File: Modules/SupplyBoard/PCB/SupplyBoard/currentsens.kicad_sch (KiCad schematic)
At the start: 8 parts

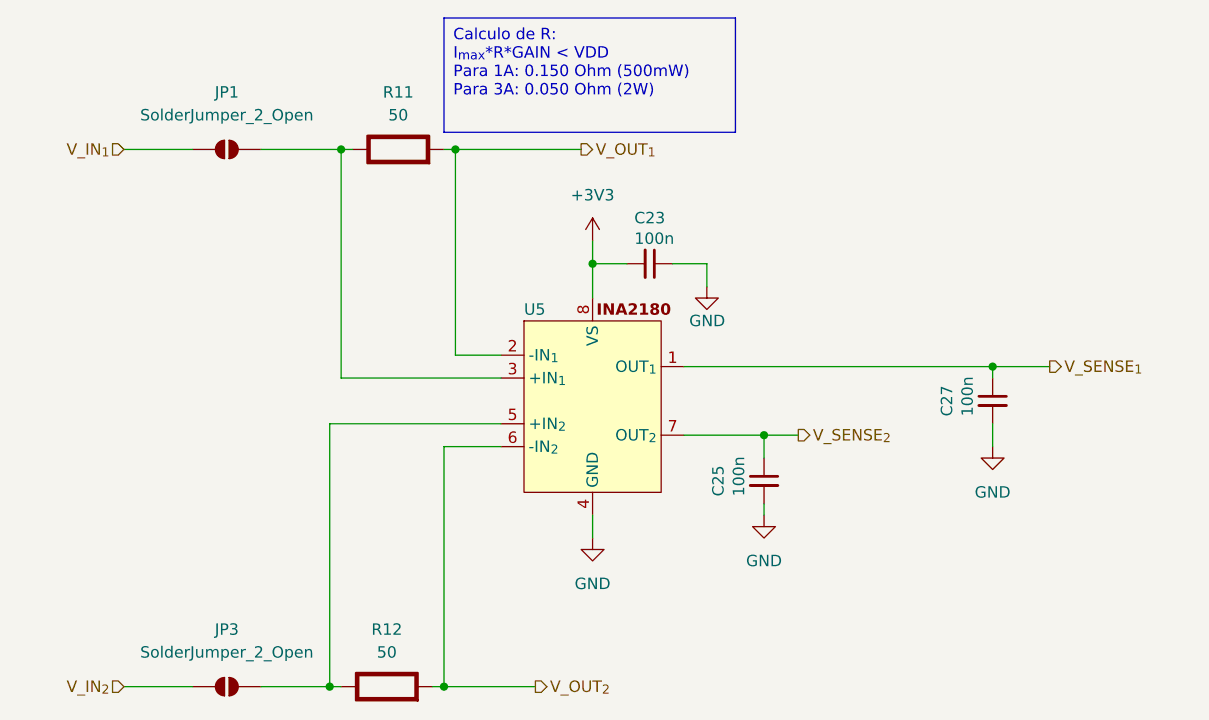
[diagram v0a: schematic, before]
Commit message: Supply board schematic and PCB
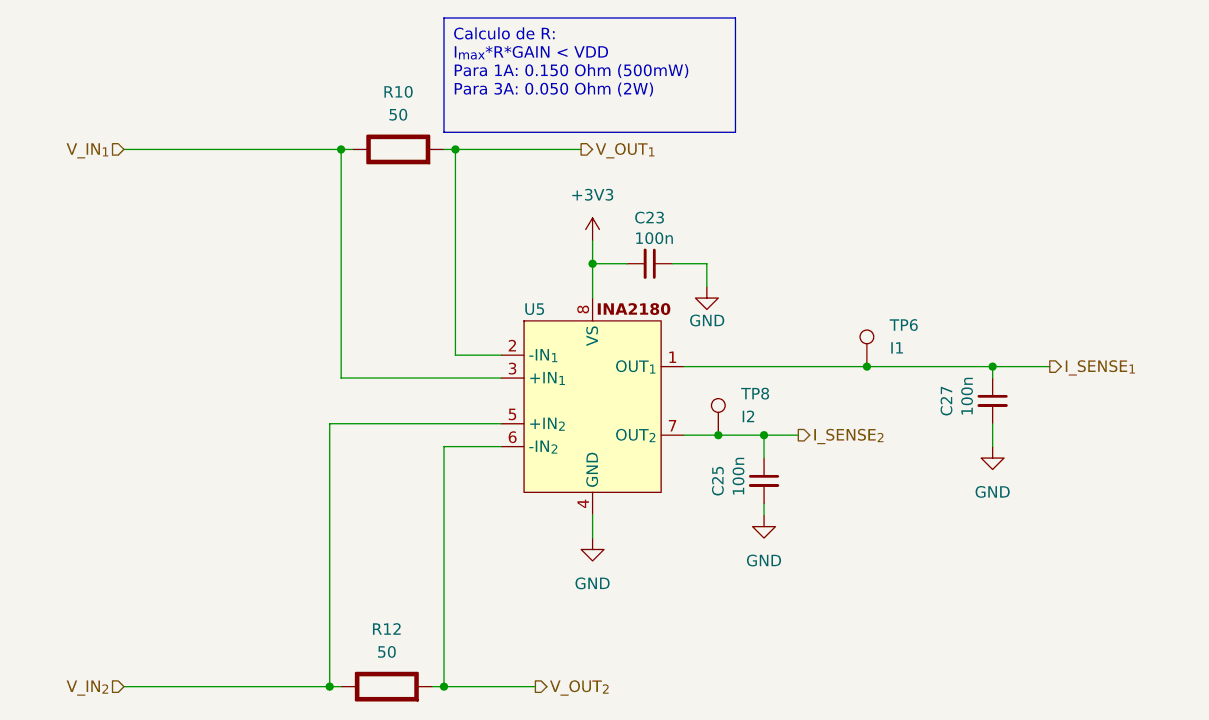
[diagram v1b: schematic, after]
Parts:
- removed JP1, JP3: SolderJumper_2_Open, Jumper:SolderJumper-2_P1.3mm_Open_RoundedPad1.0x1.5mm, symbol Jumper:SolderJumper_2_Open
- added TP6: I1, TestPoint:TestPoint_Pad_D1.5mm, symbol Connector:TestPoint
- added TP8: I2, TestPoint:TestPoint_Pad_D1.5mm, symbol Connector:TestPoint
- C23, C25, C27: footprint Capacitor_SMD:C_0805_2012Metric_Pad1.18x1.45mm_HandSolder -> Capacitor_SMD:C_0603_1608Metric_Pad1.08x0.95mm_HandSolder
- renumbered R11 to R10
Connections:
- net V_IN_{1}: now also R10.1 (+), U5.3 (+IN_{1})
- net V_IN_{2}: now also R12.1 (+), U5.5 (+IN_{2})
- net V_SENSE_{1} renamed I_SENSE_{1}
- net I_SENSE_{1}: now also TP6.1
- net V_SENSE_{2} renamed I_SENSE_{2}
- net I_SENSE_{2}: now also TP8.1
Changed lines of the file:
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@@
+	)
+	(junction
+		(at 121.92 100.33)
+		(diameter 0)
+		(color 0 0 0 0)
 	)
 	(junction
@@
 	)
 	(junction
+		(at 138.43 92.71)
+		(diameter 0)
+		(color 0 0 0 0)
+	)
+	(junction
 		(at 127 100.33)
 		(diameter 0)
@@
 	(wire
 		(pts
+			(xy 121.92 100.33) (xy 127 100.33)
+		)
+		(stroke
+			(width 0)
+			(type default)
+		)
+	)
+	(wire
+		(pts
 			(xy 127 100.33) (xy 130.81 100.33)
 		)
@@
 	(wire
 		(pts
-			(xy 55.88 68.58) (xy 63.5 68.58)
-		)
-		(stroke
-			(width 0)
-			(type default)
-		)
-	)
-	(wire
-		(pts
-			(xy 118.11 100.33) (xy 127 100.33)
-		)
-		(stroke
-			(width 0)
-			(type default)
-		)
-	)
-	(wire
-		(pts
-			(xy 55.88 128.27) (xy 63.5 128.27)
+			(xy 55.88 68.58) (xy 80.01 68.58)
+		)
+		(stroke
+			(width 0)
+			(type default)
+		)
+	)
+	(wire
+		(pts
+			(xy 118.11 100.33) (xy 121.92 100.33)
+		)
+		(stroke
+			(width 0)
+			(type default)
+		)
+	)
+	(wire
+		(pts
+			(xy 55.88 128.27) (xy 78.74 128.27)
 		)
 		(stroke
@@
 	(wire
 		(pts
-			(xy 71.12 128.27) (xy 78.74 128.27)
-		)
-		(stroke
-			(width 0)
-			(type default)
-		)
-	)
-	(wire
-		(pts
 			(xy 116.84 81.28) (xy 120.65 81.28)
 		)
@@
 	(wire
 		(pts
+			(xy 138.43 92.71) (xy 152.4 92.71)
+		)
+		(stroke
+			(width 0)
+			(type default)
+		)
+	)
+	(wire
+		(pts
 			(xy 92.71 68.58) (xy 106.68 68.58)
 		)
@@
 	(wire
 		(pts
-			(xy 71.12 68.58) (xy 80.01 68.58)
-		)
-		(stroke
-			(width 0)
-			(type default)
-		)
-	)
-	(wire
-		(pts
 			(xy 78.74 99.06) (xy 97.79 99.06)
 		)
@@
 	(wire
 		(pts
-			(xy 118.11 92.71) (xy 152.4 92.71)
+			(xy 118.11 92.71) (xy 138.43 92.71)
 		)
 		(stroke
@@
 		)
 	)
-	(hierarchical_label "V_SENSE_{1}"
+	(hierarchical_label "I_SENSE_{1}"
 		(shape output)
 		(at 158.75 92.71 0)
@@
 		)
 	)
-	(hierarchical_label "V_SENSE_{2}"
+	(hierarchical_label "I_SENSE_{2}"
 		(shape output)
 		(at 130.81 100.33 0)
@@
 			)
 		)
-		(property "Footprint" "Capacitor_SMD:C_0805_2012Metric_Pad1.18x1.45mm_HandSolder"
+		(property "Footprint" "Capacitor_SMD:C_0603_1608Metric_Pad1.08x0.95mm_HandSolder"
 			(at 114.3 81.28 0)
 			(effects
@@
 		(dnp no)
 		(fields_autoplaced yes)
-		(property "Reference" "#PWR031"
+		(property "Reference" "#PWR030"
 			(at 107.95 118.11 0)
 			(effects
@@
 	)
 	(symbol
-		(lib_id "Jumper:SolderJumper_2_Open")
-		(at 67.31 128.27 0)
-		(unit 1)
-		(exclude_from_sim yes)
-		(in_bom no)
-		(on_board yes)
-		(dnp no)
-		(fields_autoplaced yes)
-		(property "Reference" "JP3"
-			(at 67.31 121.92 0)
-			(effects
-				(font
-					(size 1.27 1.27)
-				)
-			)
-		)
-		(property "Value" "SolderJumper_2_Open"
-			(at 67.31 124.46 0)
-			(effects
-				(font
-					(size 1.27 1.27)
-				)
-			)
-		)
-		(property "Footprint" "Jumper:SolderJumper-2_P1.3mm_Open_RoundedPad1.0x1.5mm"
-			(at 67.31 128.27 0)
-			(effects
-				(font
-					(size 1.27 1.27)
-				)
-				(hide yes)
-			)
-		)
-		(property "Datasheet" "~"
-			(at 67.31 128.27 0)
-			(effects
-				(font
-					(size 1.27 1.27)
-				)
-				(hide yes)
-			)
-		)
-		(property "Description" "Solder Jumper, 2-pole, open"
-			(at 67.31 128.27 0)
-			(effects
-				(font
-					(size 1.27 1.27)
-				)
-				(hide yes)
-			)
-		)
-		(pin "2"
-		)
-		(pin "1"
-		)
-		(instances
-			(project "SupplyBoard"
-				(path "/e0885a0e-6910-46ab-84fb-bbb29c8999bc/a340e86c-d881-417a-83c0-e7c56f625c6c"
-					(reference "JP3")
-					(unit 1)
-				)
-				(path "/e0885a0e-6910-46ab-84fb-bbb29c8999bc/d9766b38-4ee2-4338-b601-caafb894792f"
-					(reference "JP4")
-					(unit 1)
-				)
-			)
-		)
-	)
-	(symbol
 		(lib_id "IcaroLib:INA2180")
 		(at 107.95 96.52 0)
@@
 			)
 		)
-		(property "Footprint" "Capacitor_SMD:C_0805_2012Metric_Pad1.18x1.45mm_HandSolder"
+		(property "Footprint" "Capacitor_SMD:C_0603_1608Metric_Pad1.08x0.95mm_HandSolder"
 			(at 152.4 96.52 0)
 			(effects
@@
 				(path "/e0885a0e-6910-46ab-84fb-bbb29c8999bc/d9766b38-4ee2-4338-b601-caafb894792f"
 					(reference "C28")
+					(unit 1)
+				)
+			)
+		)
+	)
+	(symbol
+		(lib_id "Connector:TestPoint")
+		(at 121.92 100.33 0)
+		(unit 1)
+		(exclude_from_sim no)
+		(in_bom yes)
+		(on_board yes)
+		(dnp no)
+		(fields_autoplaced yes)
+		(property "Reference" "TP8"
+			(at 124.46 95.7579 0)
+			(effects
+				(font
+					(size 1.27 1.27)
+				)
+				(justify left)
+			)
+		)
+		(property "Value" "I2"
+			(at 124.46 98.2979 0)
+			(effects
+				(font
+					(size 1.27 1.27)
+				)
+				(justify left)
+			)
+		)
+		(property "Footprint" "TestPoint:TestPoint_Pad_D1.5mm"
+			(at 127 100.33 0)
+			(effects
+				(font
+					(size 1.27 1.27)
+				)
+				(hide yes)
+			)
+		)
+		(property "Datasheet" "~"
+			(at 127 100.33 0)
+			(effects
+				(font
+					(size 1.27 1.27)
+				)
+				(hide yes)
+			)
+		)
+		(property "Description" "test point"
+			(at 121.92 100.33 0)
+			(effects
+				(font
+					(size 1.27 1.27)
+				)
+				(hide yes)
+			)
+		)
+		(pin "1"
+		)
+		(instances
+			(project "SupplyBoard"
+				(path "/e0885a0e-6910-46ab-84fb-bbb29c8999bc/a340e86c-d881-417a-83c0-e7c56f625c6c"
+					(reference "TP8")
+					(unit 1)
+				)
+				(path "/e0885a0e-6910-46ab-84fb-bbb29c8999bc/d9766b38-4ee2-4338-b601-caafb894792f"
+					(reference "TP9")
 					(unit 1)
 				)
@@
 	)
 	(symbol
-		(lib_id "Jumper:SolderJumper_2_Open")
-		(at 67.31 68.58 0)
-		(unit 1)
-		(exclude_from_sim yes)
-		(in_bom no)
-		(on_board yes)
-		(dnp no)
-		(fields_autoplaced yes)
-		(property "Reference" "JP1"
-			(at 67.31 62.23 0)
-			(effects
-				(font
-					(size 1.27 1.27)
-				)
-			)
-		)
-		(property "Value" "SolderJumper_2_Open"
-			(at 67.31 64.77 0)
-			(effects
-				(font
-					(size 1.27 1.27)
-				)
-			)
-		)
-		(property "Footprint" "Jumper:SolderJumper-2_P1.3mm_Open_RoundedPad1.0x1.5mm"
-			(at 67.31 68.58 0)
-			(effects
-				(font
-					(size 1.27 1.27)
-				)
-				(hide yes)
-			)
-		)
-		(property "Datasheet" "~"
-			(at 67.31 68.58 0)
-			(effects
-				(font
-					(size 1.27 1.27)
-				)
-				(hide yes)
-			)
-		)
-		(property "Description" "Solder Jumper, 2-pole, open"
-			(at 67.31 68.58 0)
-			(effects
-				(font
-					(size 1.27 1.27)
-				)
-				(hide yes)
-			)
-		)
-		(pin "2"
-		)
-		(pin "1"
-		)
-		(instances
-			(project ""
-				(path "/e0885a0e-6910-46ab-84fb-bbb29c8999bc/a340e86c-d881-417a-83c0-e7c56f625c6c"
-					(reference "JP1")
-					(unit 1)
-				)
-				(path "/e0885a0e-6910-46ab-84fb-bbb29c8999bc/d9766b38-4ee2-4338-b601-caafb894792f"
-					(reference "JP2")
-					(unit 1)
-				)
-			)
-		)
-	)
-	(symbol
 		(lib_id "PCM_Elektuur:R")
 		(at 86.36 68.58 90)
@@
 		(dnp no)
 		(fields_autoplaced yes)
-		(property "Reference" "R11"
+		(property "Reference" "R10"
 			(at 86.36 62.23 90)
 			(effects
@@
 				(path "/e0885a0e-6910-46ab-84fb-bbb29c8999bc/d9766b38-4ee2-4338-b601-caafb894792f"
 					(reference "R11")
+					(unit 1)
+				)
+			)
+		)
+	)
+	(symbol
+		(lib_id "Connector:TestPoint")
+		(at 138.43 92.71 0)
+		(unit 1)
+		(exclude_from_sim no)
+		(in_bom yes)
+		(on_board yes)
+		(dnp no)
+		(fields_autoplaced yes)
+		(property "Reference" "TP6"
+			(at 140.97 88.1379 0)
+			(effects
+				(font
+					(size 1.27 1.27)
+				)
+				(justify left)
+			)
+		)
+		(property "Value" "I1"
+			(at 140.97 90.6779 0)
+			(effects
+				(font
+					(size 1.27 1.27)
+				)
+				(justify left)
+			)
+		)
+		(property "Footprint" "TestPoint:TestPoint_Pad_D1.5mm"
+			(at 143.51 92.71 0)
+			(effects
+				(font
+					(size 1.27 1.27)
+				)
+				(hide yes)
+			)
+		)
+		(property "Datasheet" "~"
+			(at 143.51 92.71 0)
+			(effects
+				(font
+					(size 1.27 1.27)
+				)
+				(hide yes)
+			)
+		)
+		(property "Description" "test point"
+			(at 138.43 92.71 0)
+			(effects
+				(font
+					(size 1.27 1.27)
+				)
+				(hide yes)
+			)
+		)
+		(pin "1"
+		)
+		(instances
+			(project "SupplyBoard"
+				(path "/e0885a0e-6910-46ab-84fb-bbb29c8999bc/a340e86c-d881-417a-83c0-e7c56f625c6c"
+					(reference "TP6")
+					(unit 1)
+				)
+				(path "/e0885a0e-6910-46ab-84fb-bbb29c8999bc/d9766b38-4ee2-4338-b601-caafb894792f"
+					(reference "TP7")
 					(unit 1)
 				)
@@
 			)
 		)
-		(property "Footprint" "Capacitor_SMD:C_0805_2012Metric_Pad1.18x1.45mm_HandSolder"
+		(property "Footprint" "Capacitor_SMD:C_0603_1608Metric_Pad1.08x0.95mm_HandSolder"
 			(at 127 105.41 0)
 			(effects

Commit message: Updated supply board for v2, and BMP280 tinkering project
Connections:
- net +3V3 renamed +3.3V
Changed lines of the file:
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@@
 (kicad_sch
-	(version 20231120)
+	(version 20250114)
 	(generator "eeschema")
-	(generator_version "8.0")
+	(generator_version "9.0")
 	(paper "A4")
+	(text_box "Calculo de R:\nI_{max}*R*GAIN < VDD\nPara 1A: 0.150 Ohm (500mW)\nPara 3A: 0.050 Ohm (2W)"
+		(exclude_from_sim no)
+		(at 91.44 53.975 0)
+		(size 32.385 12.7)
+		(margins 0.9525 0.9525 0.9525 0.9525)
+		(stroke
+			(width 0)
+			(type default)
+		)
+		(fill
+			(type none)
+		)
+		(effects
+			(font
+				(size 1.27 1.27)
+			)
+			(justify left top)
+		)
+	)
 	(junction
 		(at 92.71 68.58)
@@
 			(width 0)
 			(type default)
-		)
-	)
-	(text_box "Calculo de R:\nI_{max}*R*GAIN < VDD\nPara 1A: 0.150 Ohm (500mW)\nPara 3A: 0.050 Ohm (2W)"
-		(exclude_from_sim no)
-		(at 91.44 53.975 0)
-		(size 32.385 12.7)
-		(stroke
-			(width 0)
-			(type default)
-		)
-		(fill
-			(type none)
-		)
-		(effects
-			(font
-				(size 1.27 1.27)
-			)
-			(justify left top)
 		)
 	)
@@
 	)
 	(symbol
+		(lib_id "power:+3.3V")
+		(at 107.95 78.74 0)
+		(unit 1)
+		(exclude_from_sim no)
+		(in_bom yes)
+		(on_board yes)
+		(dnp no)
+		(fields_autoplaced yes)
+		(property "Reference" "#PWR028"
+			(at 107.95 82.55 0)
+			(effects
+				(font
+					(size 1.27 1.27)
+				)
+				(hide yes)
+			)
+		)
+		(property "Value" "+3.3V"
+			(at 107.95 73.66 0)
+			(effects
+				(font
+					(size 1.27 1.27)
+				)
+			)
+		)
+		(property "Footprint" ""
+			(at 107.95 78.74 0)
+			(effects
+				(font
+					(size 1.27 1.27)
+				)
+				(hide yes)
+			)
+		)
+		(property "Datasheet" ""
+			(at 107.95 78.74 0)
+			(effects
+				(font
+					(size 1.27 1.27)
+				)
+				(hide yes)
+			)
+		)
+		(property "Description" "Power symbol creates a global label with name \"+3.3V\""
+			(at 107.95 78.74 0)
+			(effects
+				(font
+					(size 1.27 1.27)
+				)
+				(hide yes)
+			)
+		)
+		(pin "1"
+		)
+		(instances
+			(project "SupplyBoard"
+				(path "/e0885a0e-6910-46ab-84fb-bbb29c8999bc/a340e86c-d881-417a-83c0-e7c56f625c6c"
+					(reference "#PWR028")
+					(unit 1)
+				)
+				(path "/e0885a0e-6910-46ab-84fb-bbb29c8999bc/d9766b38-4ee2-4338-b601-caafb894792f"
+					(reference "#PWR029")
+					(unit 1)
+				)
+			)
+		)
+	)
+	(symbol
 		(lib_id "Connector:TestPoint")
 		(at 121.92 100.33 0)
@@
 					(unit 1)
 				)
-			)
-		)
-	)
-	(symbol
-		(lib_id "power:+3V3")
-		(at 107.95 78.74 0)
-		(unit 1)
-		(exclude_from_sim no)
-		(in_bom yes)
-		(on_board yes)
-		(dnp no)
-		(fields_autoplaced yes)
-		(property "Reference" "#PWR028"
-			(at 107.95 82.55 0)
-			(effects
-				(font
-					(size 1.27 1.27)
-				)
-				(hide yes)
-			)
-		)
-		(property "Value" "+3V3"
-			(at 107.95 73.66 0)
-			(effects
-				(font
-					(size 1.27 1.27)
-				)
-			)
-		)
-		(property "Footprint" ""
-			(at 107.95 78.74 0)
-			(effects
-				(font
-					(size 1.27 1.27)
-				)
-				(hide yes)
-			)
-		)
-		(property "Datasheet" ""
-			(at 107.95 78.74 0)
-			(effects
-				(font
-					(size 1.27 1.27)
-				)
-				(hide yes)
-			)
-		)
-		(property "Description" "Power symbol creates a global label with name \"+3V3\""
-			(at 107.95 78.74 0)
-			(effects
-				(font
-					(size 1.27 1.27)
-				)
-				(hide yes)
-			)
-		)
-		(pin "1"
-		)
-		(instances
-			(project ""
-				(path "/e0885a0e-6910-46ab-84fb-bbb29c8999bc/a340e86c-d881-417a-83c0-e7c56f625c6c"
-					(reference "#PWR028")
-					(unit 1)
-				)
-				(path "/e0885a0e-6910-46ab-84fb-bbb29c8999bc/d9766b38-4ee2-4338-b601-caafb894792f"
-					(reference "#PWR029")
-					(unit 1)
-				)
